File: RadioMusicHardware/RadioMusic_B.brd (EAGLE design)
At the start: 107 x 19.5 mm, 33 parts, among them IC4 TL074, U1 TEENSY_3.1_TW

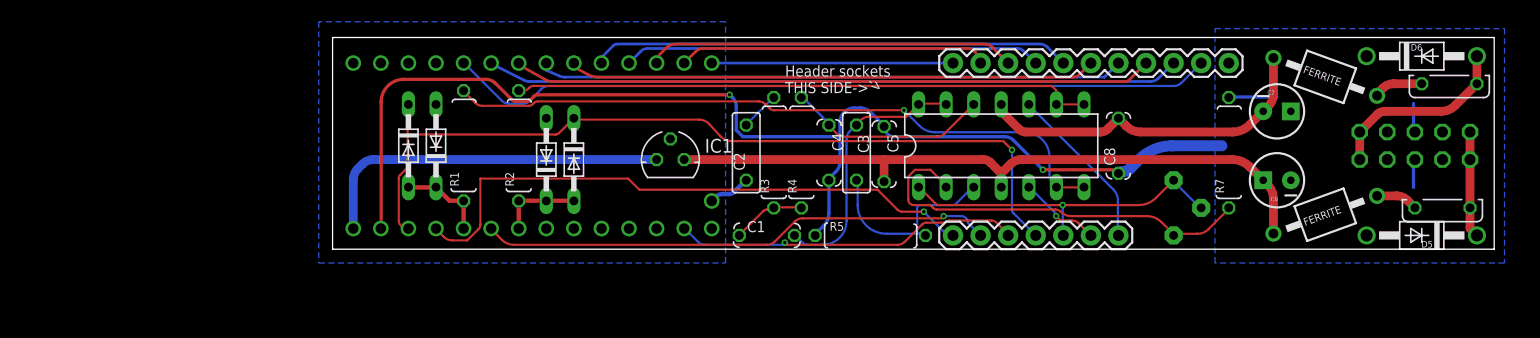
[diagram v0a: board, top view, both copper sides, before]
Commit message: Revision 3 front and back PCBs sent to Fab
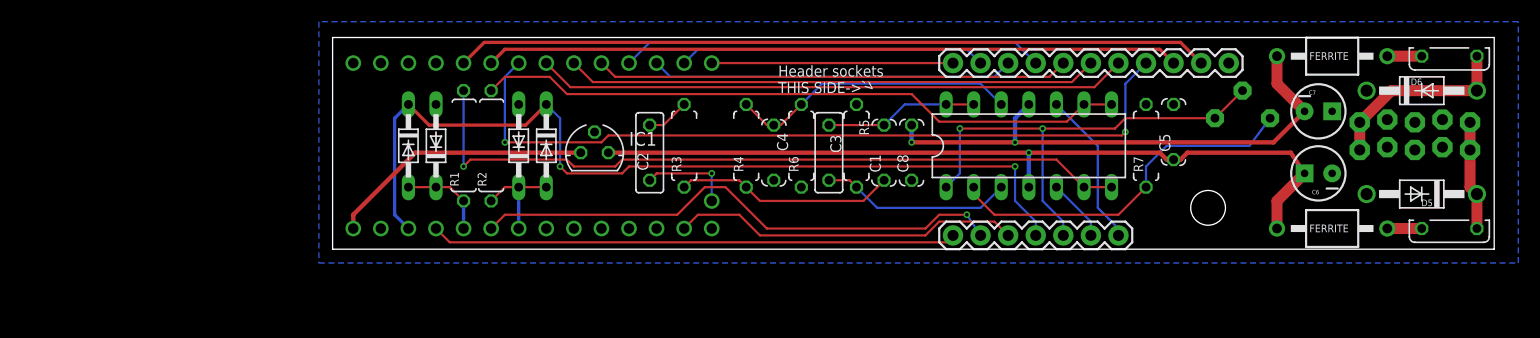
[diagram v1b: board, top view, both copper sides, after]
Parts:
- removed U$4: (no value), TW_logos:MTM_2CM
- added R6: 100k, MusicThingModular:7MM_RESISTOR
- added U$1: (no value), MusicThingModular:MOUNTING_HOLE
- R3, R4, R5, R7: device TomW:0207/10 -> MusicThingModular:7MM_RESISTOR
- SV1: value (none) -> EURO_POWER_HEADERLOCK_PADS; device TomW:MA05-2 -> MusicThingModular:EURO_PWR_HEADER_LOCK
- moved C5 26.7 mm to (77.5, 10.8), turned to 90 degrees
- moved C8 19.1 mm to (53.3, 8.89)
- moved U$2 16.5 mm to (53.6, 12.5), turned to 0 degrees
- moved C1 13.2 mm to (50.8, 8.89), turned to 90 degrees
- moved OUTPUT 10.4 mm to (83.8, 12.1), turned to 0 degrees
- moved C2 8.89 mm to (29.2, 8.89)
- moved R5 8.35 mm to (48.3, 9.53), turned to 270 degrees
- moved R3 8.28 mm to (32.4, 9.53)
- moved R7 7.65 mm to (74.9, 9.53)
- moved IC1 7.01 mm to (24.1, 8.89)
- moved R4 5.12 mm to (38.1, 9.53)
- moved C4 5.08 mm to (40.6, 8.89)
- moved C6 3.86 mm to (90.8, 6.99)
- moved C7 3.81 mm to (90.8, 12.7)
- moved D5 3.81 mm to (100.3, 5.08)
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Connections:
- removed net DGND: D2.A, D4.A, IC1.GND, U1.GND
- net +12V: now also C5.1; no longer C5.2
- net +12V_INLET: now also SV1.POS1, SV1.POS2; no longer SV1.10, SV1.9
- net -12V_INLET: now also SV1.NEG1, SV1.NEG2; no longer SV1.1, SV1.2
- net GND: now also C5.2, D2.A, D4.A, IC1.GND, R6.1, SV1.GND1, SV1.GND2, SV1.GND3, SV1.GND4, SV1.GND5, SV1.GND6, U1.GND; no longer C5.1, SV1.3, SV1.4, SV1.5, SV1.6, SV1.7, SV1.8
- net N$2: now also R6.2
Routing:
- net GND: track 118.8 -> 0.00 mm, vias 2 -> 0
- net -12V: track 32.2 -> 49.1 mm, vias 0 -> 2
- net LED3: track 59.0 -> 72.5 mm, vias 0 -> 2
- net N$4: track 6.89 -> 20.3 mm
- net AUDIO_OUT: track 31.4 -> 44.0 mm, vias 1 -> 2
- net +12V: track 63.4 -> 75.0 mm, vias 0 -> 1
- net N$5: track 24.3 -> 14.1 mm
- net +5V: track 33.4 -> 24.6 mm
- net N$2: track 18.7 -> 26.7 mm
- net CHANNEL_POT: track 55.1 -> 48.4 mm, vias 1 -> 0
- net N$3: track 62.1 -> 68.5 mm
- net N$1: track 53.6 -> 60.0 mm
- net DAC: track 3.86 -> 8.52 mm, vias 0 -> 1
- net N$7: track 38.2 -> 33.7 mm
- net +3.3V: track 78.3 -> 82.6 mm, vias 1 -> 2
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- removed copper zone on layer 16, net DGND
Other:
- board text added: "November 2015 musicthing.co.uk CC-BY-SA"
- board text added: "RED>RED>RED"
- board text added: "Radio Music Back PCB Rev3 Designed in Herne Hill, London by Tom Whitwell"
- board text added: "or 3.2"
- board text removed: "December 2014 musicthing.co.uk CC-BY-SA"
- board text removed: "Radio Music Back PCB Rev2 Designed in Herne Hill, London by Tom Whitwell"

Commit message: 3.1 Hardware Finalised
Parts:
- R1, R2: value 47R -> 1k
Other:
- board text added: "Radio Music Back PCB Rev3.1 Designed in Herne Hill, London by Tom Whitwell"
- board text removed: "Radio Music Back PCB Rev3 Designed in Herne Hill, London by Tom Whitwell"

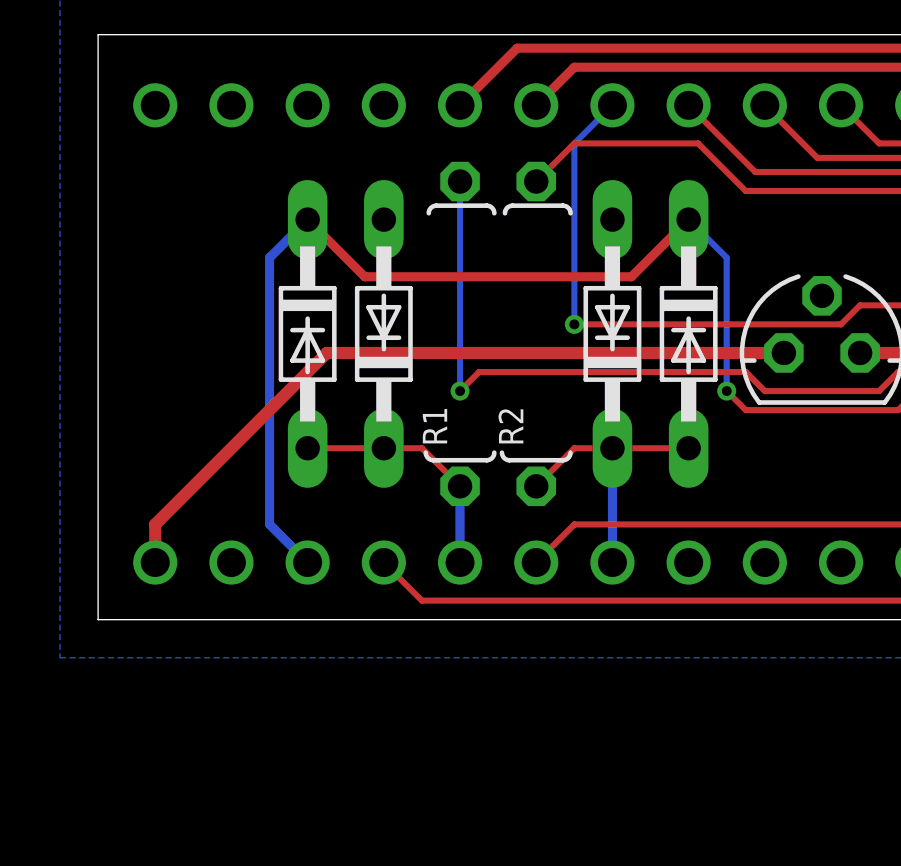
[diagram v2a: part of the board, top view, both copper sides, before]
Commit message: Layout experiments - back board output not completed
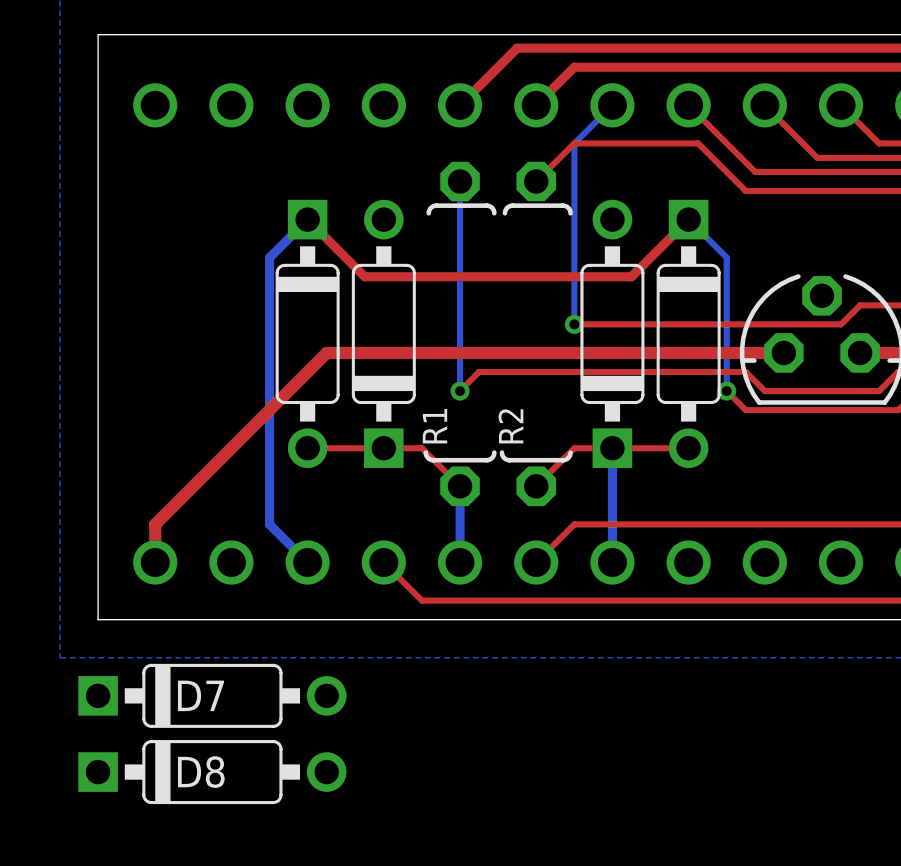
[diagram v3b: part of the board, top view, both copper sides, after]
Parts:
- added D7, D8: BAT42, MusicThingModular:DO35-7
- D1, D2, D3, D4: device diode:DO34-7 -> MusicThingModular:DO35-7
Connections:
- net +3.3V: now also D7.C
- net GND: now also D8.A
- net RESET_CV: now also D7.A, D8.C
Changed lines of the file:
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@@
 <?xml version="1.0" encoding="utf-8"?>
 <!DOCTYPE eagle SYSTEM "eagle.dtd">
-<eagle version="7.2.0">
+<eagle version="7.4.0">
 <drawing>
 <settings>
@@
 <layer number="14" name="Route14" color="1" fill="6" visible="no" active="no"/>
 <layer number="15" name="Route15" color="4" fill="6" visible="no" active="yes"/>
-<layer number="16" name="Bottom" color="1" fill="1" visible="no" active="yes"/>
-<layer number="17" name="Pads" color="2" fill="1" visible="no" active="yes"/>
-<layer number="18" name="Vias" color="2" fill="1" visible="no" active="yes"/>
+<layer number="16" name="Bottom" color="1" fill="1" visible="yes" active="yes"/>
+<layer number="17" name="Pads" color="2" fill="1" visible="yes" active="yes"/>
+<layer number="18" name="Vias" color="2" fill="1" visible="yes" active="yes"/>
 <layer number="19" name="Unrouted" color="6" fill="1" visible="no" active="yes"/>
 <layer number="20" name="Dimension" color="15" fill="1" visible="no" active="yes"/>
@@
 </element>
 <element name="U1" library="TomW" package="TEENSY_3.1_TW" value="TEENSY_3.1_TW" x="18.415" y="9.525" smashed="yes" rot="MR270"/>
-<element name="D1" library="diode" package="DO34-7" value="BAT42" x="6.985" y="9.525" smashed="yes" rot="R270">
+<element name="D1" library="MusicThingModular" package="DO35-7" value="BAT42" x="6.985" y="9.525" smashed="yes" rot="R270">
 <attribute name="VALUE" x="4.572" y="12.6746" size="1.27" layer="27" ratio="10" rot="R270"/>
 </element>
-<element name="D2" library="diode" package="DO34-7" value="BAT42" x="9.525" y="9.525" smashed="yes" rot="R90"/>
+<element name="D2" library="MusicThingModular" package="DO35-7" value="BAT42" x="9.525" y="9.525" smashed="yes" rot="R90"/>
 <element name="R4" library="MusicThingModular" package="7MM_RESISTOR" value="8.2k" x="38.1" y="9.525" rot="R90"/>
 <element name="R3" library="MusicThingModular" package="7MM_RESISTOR" value="8.2k" x="32.385" y="9.525" rot="R90"/>
@@
 <element name="C2" library="TomW" package="C050-025X075" value="100n" x="29.21" y="8.89" rot="R90"/>
 <element name="R1" library="TomW" package="0207/10" value="1k" x="12.065" y="9.525" rot="R90"/>
-<element name="D3" library="diode" package="DO34-7" value="BAT42" x="19.685" y="9.525" smashed="yes" rot="R270"/>
-<element name="D4" library="diode" package="DO34-7" value="BAT42" x="17.145" y="9.525" smashed="yes" rot="R90">
+<element name="D3" library="MusicThingModular" package="DO35-7" value="BAT42" x="19.685" y="9.525" smashed="yes" rot="R270"/>
+<element name="D4" library="MusicThingModular" package="DO35-7" value="BAT42" x="17.145" y="9.525" smashed="yes" rot="R90">
 <attribute name="VALUE" x="21.9964" y="6.3754" size="1.27" layer="27" ratio="10" rot="R90"/>
 </element>
@@
 <element name="R6" library="MusicThingModular" package="7MM_RESISTOR" value="100k" x="43.18" y="9.525" rot="R90"/>
 <element name="U$1" library="MusicThingModular" package="MOUNTING_HOLE" value="" x="80.645" y="3.81"/>
+<element name="D7" library="MusicThingModular" package="DO35-7" value="BAT42" x="3.81" y="-2.54"/>
+<element name="D8" library="MusicThingModular" package="DO35-7" value="BAT42" x="3.81" y="-5.08"/>
 </elements>
 <signals>
@@
 <vertex x="-1.27" y="20.955"/>
 </polygon>
+<contactref element="D8" pad="A"/>
+<wire x1="99.695" y1="11.684" x2="102.235" y2="11.938" width="0" layer="19" extent="1-1"/>
+<wire x1="102.235" y1="9.398" x2="102.235" y2="11.938" width="0" layer="19" extent="1-1"/>
+<wire x1="97.155" y1="11.938" x2="99.695" y2="11.684" width="0" layer="19" extent="1-1"/>
+<wire x1="99.695" y1="9.144" x2="99.695" y2="11.684" width="0" layer="19" extent="1-1"/>
+<wire x1="97.155" y1="9.398" x2="97.155" y2="11.938" width="0" layer="19" extent="1-1"/>
+<wire x1="95.25" y1="14.605" x2="97.155" y2="11.938" width="0" layer="19" extent="1-1"/>
+<wire x1="92.075" y1="12.7" x2="95.25" y2="14.605" width="0" layer="19" extent="1-1"/>
+<wire x1="95.25" y1="5.08" x2="97.155" y2="9.398" width="0" layer="19" extent="1-1"/>
+<wire x1="92.075" y1="6.985" x2="95.25" y2="5.08" width="0" layer="19" extent="1-1"/>
+<wire x1="82.55" y1="17.145" x2="92.075" y2="12.7" width="0" layer="19" extent="1-1"/>
+<wire x1="77.47" y1="13.335" x2="82.55" y2="17.145" width="0" layer="19" extent="1-1"/>
+<wire x1="74.93" y1="13.335" x2="77.47" y2="13.335" width="0" layer="19" extent="1-1"/>
+<wire x1="53.34" y1="6.35" x2="74.93" y2="13.335" width="0" layer="19" extent="1-1"/>
+<wire x1="48.26" y1="13.335" x2="53.34" y2="6.35" width="0" layer="19" extent="1-1"/>
+<wire x1="43.18" y1="5.715" x2="48.26" y2="13.335" width="0" layer="19" extent="1-1"/>
+<wire x1="40.64" y1="6.35" x2="43.18" y2="5.715" width="0" layer="19" extent="1-1"/>
+<wire x1="24.13" y1="10.795" x2="40.64" y2="6.35" width="0" layer="19" extent="1-1"/>
+<wire x1="17.145" y1="13.335" x2="24.13" y2="10.795" width="0" layer="19" extent="1-1"/>
+<wire x1="9.525" y1="13.335" x2="17.145" y2="13.335" width="0" layer="19" extent="1-1"/>
+<wire x1="1.905" y1="17.145" x2="9.525" y2="13.335" width="0" layer="19" extent="1-1"/>
+<wire x1="4.445" y1="1.905" x2="9.525" y2="13.335" width="0" layer="19" extent="1-1"/>
+<wire x1="7.62" y1="-5.08" x2="4.445" y2="1.905" width="0" layer="19" extent="1-1"/>
 </signal>
 <signal name="+12V" class="1">
@@
 <wire x1="8.89" y1="11.43" x2="17.78" y2="11.43" width="0.3048" layer="1"/>
 <wire x1="17.78" y1="11.43" x2="19.685" y2="13.335" width="0.3048" layer="1"/>
+<contactref element="D7" pad="C"/>
+<wire x1="0" y1="-2.54" x2="5.715" y2="3.175" width="0" layer="19" extent="16-16"/>
 </signal>
 <signal name="CHANNEL_CV">
@@
 <wire x1="29.21" y1="19.05" x2="62.865" y2="19.05" width="0.2032" layer="16"/>
 <wire x1="62.865" y1="19.05" x2="64.77" y2="17.145" width="0.2032" layer="16"/>
+<contactref element="D7" pad="A"/>
+<contactref element="D8" pad="C"/>
+<wire x1="7.62" y1="-2.54" x2="27.305" y2="17.145" width="0" layer="19" extent="1-1"/>
+<wire x1="0" y1="-5.08" x2="7.62" y2="-2.54" width="0" layer="19" extent="1-1"/>
 </signal>
 <signal name="SCLK">

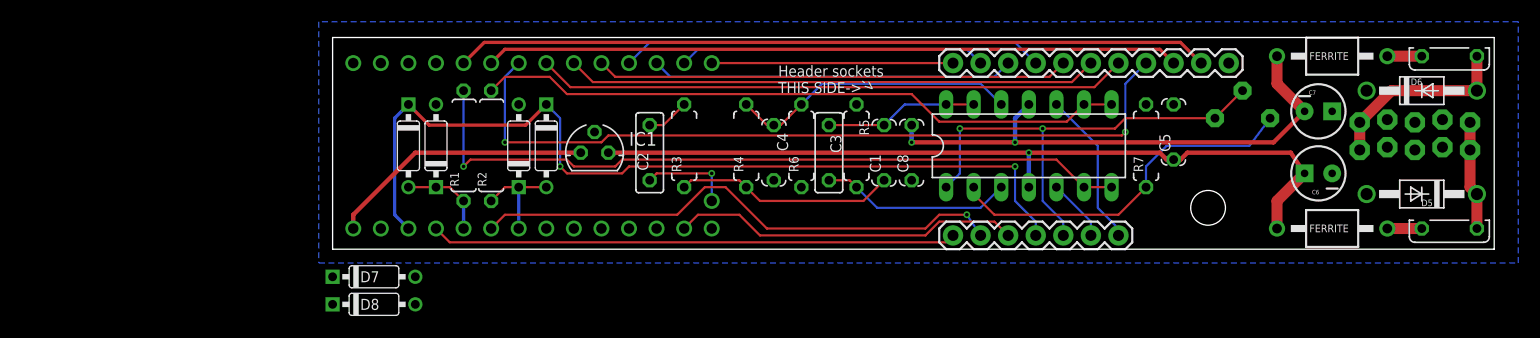
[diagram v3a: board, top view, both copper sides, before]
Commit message: schematic complete, rear not laid out
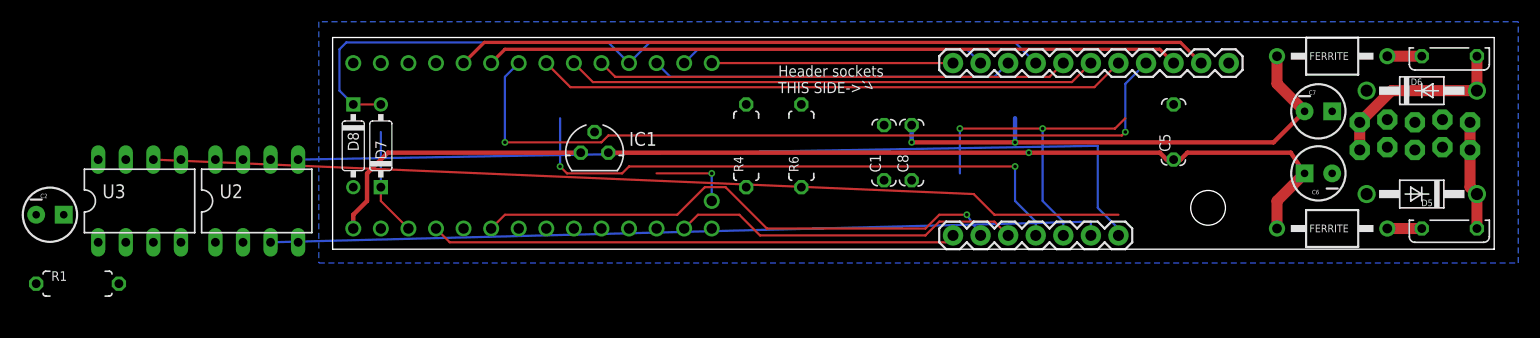
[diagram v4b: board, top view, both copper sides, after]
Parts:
- removed C3: 100n, TomW:C050-025X075
- removed C4: 1n, TomW:C050-024X044
- removed D1, D2, D3, D4: BAT42, MusicThingModular:DO35-7
- removed IC4: TL074, linear:DIL14
- removed OUTPUT: 50k, bourns:3362P
- removed R2: 1k, TomW:0207/10
- removed R3: 8.2k, MusicThingModular:7MM_RESISTOR
- removed R5: 330K, MusicThingModular:7MM_RESISTOR
- removed R7: 1k, MusicThingModular:7MM_RESISTOR
- added U2: MCP6002, MusicThingModular:DIL08
- added U3: TL072_, MusicThingModular:DIL08
- C1: value 1n -> 18p
- C2: value 100n -> 10uf; device TomW:C050-025X075 -> SparkFun-Passives:CPOL-RADIAL-10UF-25V
- R1: value 1k -> 39k; device TomW:0207/10 -> MusicThingModular:7MM_RESISTOR
- R4: value 8.2k -> 5.6k
- R6: value 100k -> 39k
- moved C2 55.5 mm to (-26.0, 3.17), turned to 0 degrees
- moved R1 37.8 mm to (-23.5, -3.17), turned to 0 degrees
- moved D8 14.7 mm to (1.91, 9.53), turned to 270 degrees
- moved D7 12.1 mm to (4.45, 9.53), turned to 90 degrees
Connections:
- removed net N$10: C2.2, R3.2
- removed net N$2: C4.1, IC4.12, R4.2, R6.2
- removed net N$3: IC4.6, IC4.7, R1.2
- removed net N$5: C1.2, C3.1, IC4.13, IC4.14
- removed net N$6: C3.2, IC4.3, R5.2
- net +12V: now also U3.8; no longer IC4.4
- net +3.3V: now also U2.8; no longer D1.C, D3.C
- net -12V: now also U3.4; no longer IC4.11
- net AUDIO_OUT: now also C1.2, R6.2, U3.1; no longer IC4.1, OUTPUT.2, OUTPUT.3
- net CHANNEL_CV: now also U2.3; no longer IC4.5
- net GND: now also U2.4, U3.3, U3.5; no longer C4.2, D2.A, D4.A, R5.1, R6.1, R7.2
- net N$1: now also C2.2, R1.2, R4.1; no longer IC4.8, IC4.9, R2.2
- net N$4: now also R4.2, R6.1, U3.2; no longer R3.1, R4.1
- net N$7: now also U3.6, U3.7; no longer IC4.2, OUTPUT.1, R7.1
- net PIN20/A6: now also U2.6, U2.7; no longer D3.A, D4.C, R2.1
- net PIN22/A8: now also U2.1, U2.2; no longer D1.A, D2.C, R1.1
- net TIME_CV: now also U2.5; no longer IC4.10
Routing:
- net CHANNEL_CV: track 5.76 -> 76.9 mm
- net N$3: track 68.5 -> 0.00 mm, vias 1 -> 0
- net TIME_CV: track 14.4 -> 82.7 mm
- net N$1: track 60.0 -> 0.00 mm
- net N$7: track 33.7 -> 89.8 mm
- net RESET_CV: track 39.0 -> 74.9 mm
- net N$2: track 26.7 -> 0.00 mm
- net N$4: track 20.3 -> 0.00 mm
- net +3.3V: track 82.6 -> 64.0 mm
- net N$6: track 17.7 -> 0.00 mm
- net N$5: track 14.1 -> 0.00 mm
- net AUDIO_OUT: track 44.0 -> 30.4 mm
- net PIN20/A6: track 9.42 -> 0.00 mm
- net PIN22/A8: track 8.15 -> 0.00 mm
- net N$10: track 3.96 -> 0.00 mm
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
